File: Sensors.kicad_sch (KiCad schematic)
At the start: 10 parts, among them U10 LSM6DSO32, U11 LIS2MDL, U12 MS5611-01BA

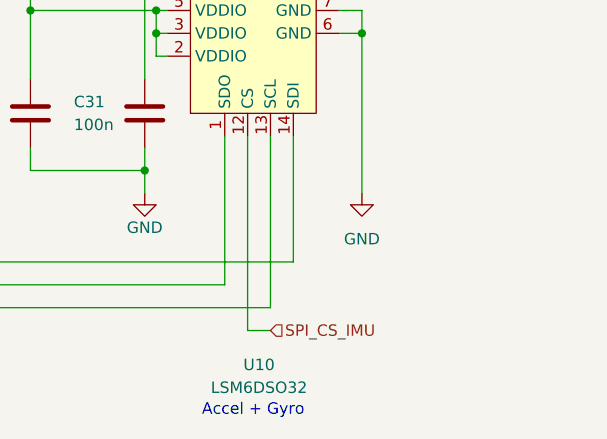
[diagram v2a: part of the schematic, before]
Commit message: :children_crossing: Add test pads and assign footprints
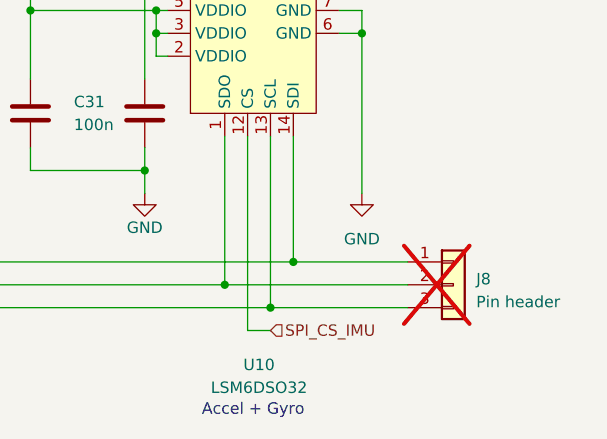
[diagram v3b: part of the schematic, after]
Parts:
- added J8: Pin header, Connector_PinHeader_2.54mm:PinHeader_1x03_P2.54mm_Vertical, symbol Connector_Generic:Conn_01x03
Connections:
- net SPI_MISO: now also J8.2 (Pin_2)
- net SPI_MOSI: now also J8.1 (Pin_1)
- net SPI_SCK: now also J8.3 (Pin_3)
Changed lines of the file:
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@@
   (junction (at 180.34 91.44) (diameter 0) (color 0 0 0 0)
   )
+  (junction (at 201.93 121.92) (diameter 0) (color 0 0 0 0)
+  )
+  (junction (at 207.01 124.46) (diameter 0) (color 0 0 0 0)
+  )
   (junction (at 193.04 88.9) (diameter 0) (color 0 0 0 0)
   )
@@
   )
   (junction (at 194.31 93.98) (diameter 0) (color 0 0 0 0)
+  )
+  (junction (at 209.55 119.38) (diameter 0) (color 0 0 0 0)
   )
   (junction (at 142.24 121.92) (diameter 0) (color 0 0 0 0)
@@
     (stroke (width 0) (type default))
   )
+  (wire (pts (xy 201.93 121.92) (xy 222.25 121.92))
+    (stroke (width 0) (type default))
+  )
   (wire (pts (xy 194.31 91.44) (xy 195.58 91.44))
     (stroke (width 0) (type default))
   )
+  (wire (pts (xy 207.01 124.46) (xy 222.25 124.46))
+    (stroke (width 0) (type default))
+  )
   (wire (pts (xy 58.42 99.06) (xy 58.42 96.52))
     (stroke (width 0) (type default))
@@
   )
   (wire (pts (xy 207.01 105.41) (xy 207.01 124.46))
+    (stroke (width 0) (type default))
+  )
+  (wire (pts (xy 209.55 119.38) (xy 222.25 119.38))
     (stroke (width 0) (type default))
   )
@@
         )
       )
+    )
+  )
+  (symbol (lib_id "Connector_Generic:Conn_01x03") (at 227.33 121.92 0) (unit 1)
+    (in_bom yes) (on_board yes) (dnp yes) (fields_autoplaced)
+    (property "Reference" "J8" (at 229.87 121.285 0)
+      (effects (font (size 1.27 1.27)) (justify left))
+    )
+    (property "Value" "Pin header" (at 229.87 123.825 0)
+      (effects (font (size 1.27 1.27)) (justify left))
+    )
+    (property "Footprint" "Connector_PinHeader_2.54mm:PinHeader_1x03_P2.54mm_Vertical" (at 227.33 121.92 0)
+      (effects (font (size 1.27 1.27)) hide)
+    )
+    (property "Datasheet" "~" (at 227.33 121.92 0)
+      (effects (font (size 1.27 1.27)) hide)
+    )
+    (pin "1")
+    (pin "2")
+    (pin "3")
+    (instances
+      (project "Nova"
+        (path "/0c006d9f-ae30-49aa-ab15-ff0bec4de0e8/b4564e06-ae37-4733-9020-dc4bb7ce2d2c"
+          (reference "J8") (unit 1)
+        )
+      )
